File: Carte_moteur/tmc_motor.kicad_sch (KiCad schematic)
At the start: 13 parts, among them J201 Conn_01x05_Pin, J202 Conn_01x04_Pin, SW201 SW_DIP_x02, U201 TMC2209

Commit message: updated motor PCB
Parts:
- removed R205: R_US, Resistor_SMD:R_0603_1608Metric_Pad0.98x0.95mm_HandSolder, symbol Device:R_US
- removed SW201: SW_DIP_x02, Button_Switch_THT:SW_DIP_SPSTx02_Slide_9.78x7.26mm_W7.62mm_P2.54mm, symbol Switch:SW_DIP_x02
- added R210, R211, R212: R_US, Resistor_SMD:R_0603_1608Metric_Pad0.98x0.95mm_HandSolder, symbol Device:R_US
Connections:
- net +3V3: now also R210.2, R211.2, R212.2
- net A: now also R210.1
- net B: now also R211.1
- net I: now also R212.1
- net UART: now also U201.4 (PDN)

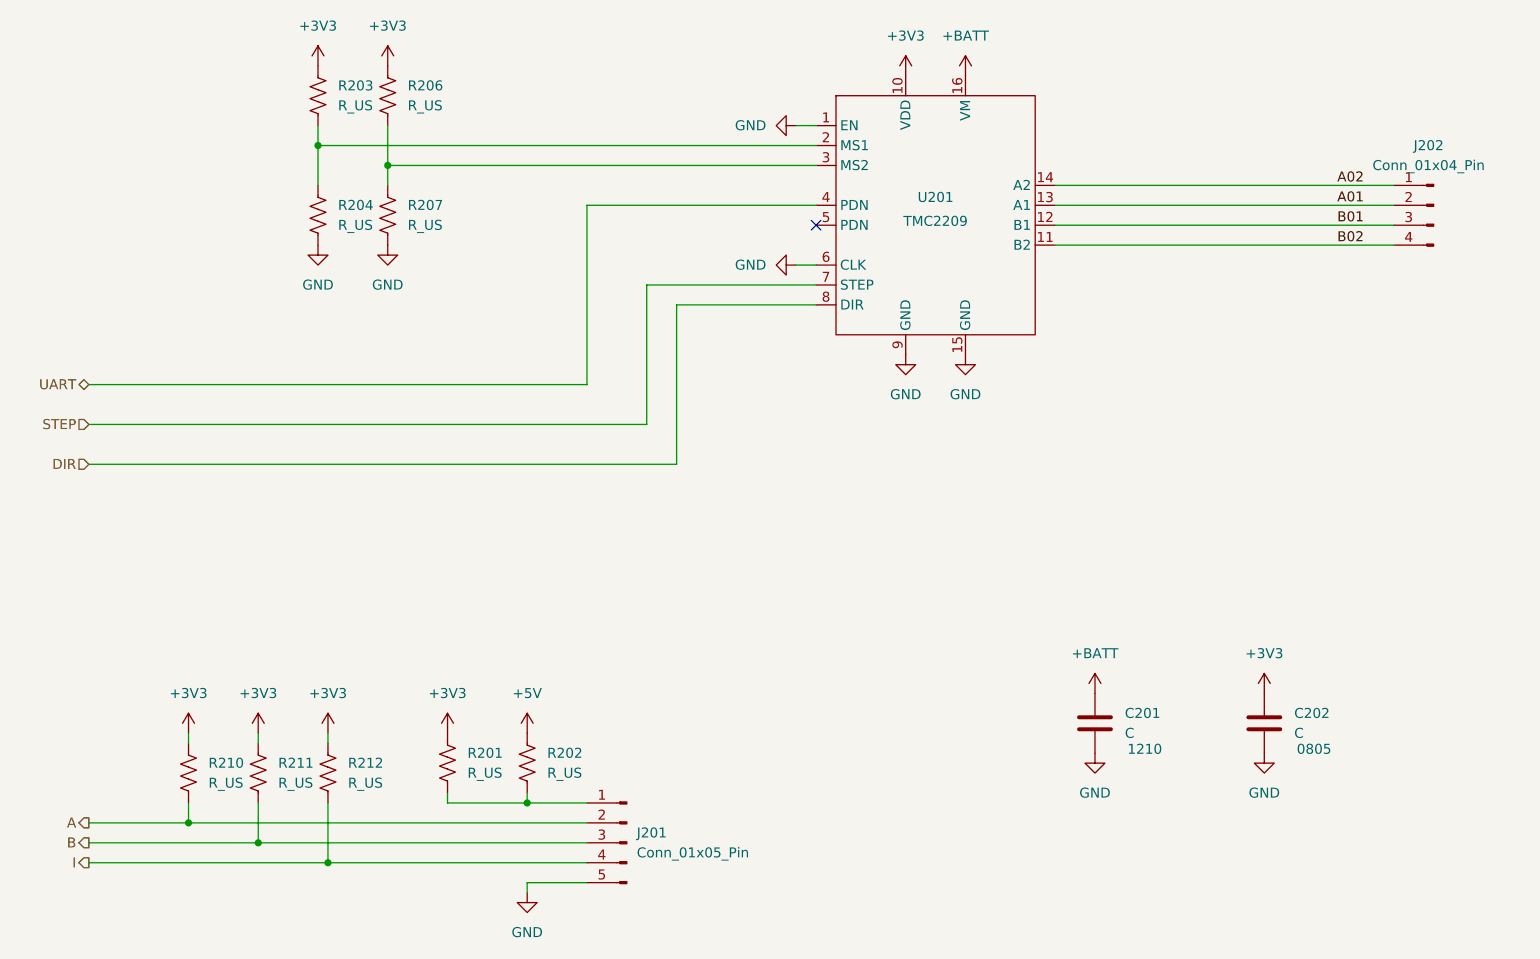
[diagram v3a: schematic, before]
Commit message: update motor board values
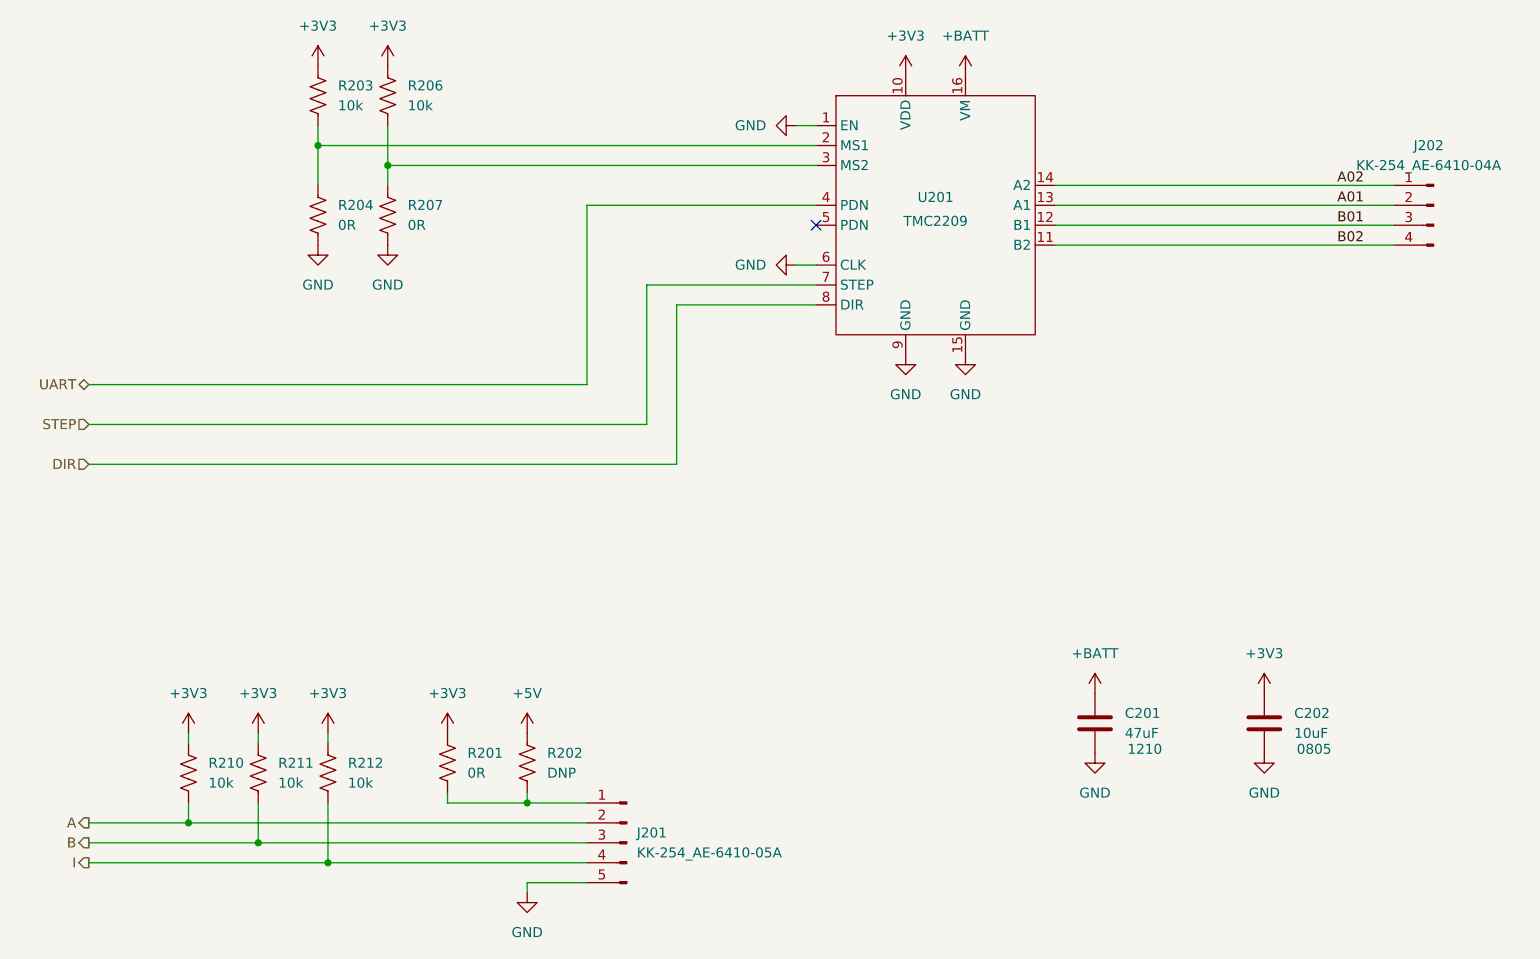
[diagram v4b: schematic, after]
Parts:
- C201: value C -> 47uF
- C202: value C -> 10uF
- J201: value Conn_01x05_Pin -> KK-254_AE-6410-05A
- J202: value Conn_01x04_Pin -> KK-254_AE-6410-04A
- R201, R204, R207: value R_US -> 0R
- R202: value R_US -> DNP
- R203, R206, R210, R211, R212: value R_US -> 10k
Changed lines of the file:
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@@
 			)
 		)
-		(property "Value" "R_US"
+		(property "Value" "10k"
 			(at 72.39 153.6699 0)
 			(effects
@@
 			)
 		)
-		(property "Value" "R_US"
+		(property "Value" "0R"
 			(at 105.41 152.3999 0)
 			(effects
@@
 			)
 		)
-		(property "Value" "R_US"
+		(property "Value" "10k"
 			(at 97.79 67.3099 0)
 			(effects
@@
 			)
 		)
-		(property "Value" "C"
+		(property "Value" "10uF"
 			(at 210.82 147.3199 0)
 			(effects
@@
 			)
 		)
-		(property "Value" "Conn_01x05_Pin"
+		(property "Value" "KK-254_AE-6410-05A"
 			(at 127 162.5599 0)
 			(effects
@@
 			)
 		)
-		(property "Value" "R_US"
+		(property "Value" "0R"
 			(at 97.79 82.5499 0)
 			(effects
@@
 			)
 		)
-		(property "Value" "R_US"
+		(property "Value" "DNP"
 			(at 115.57 152.3999 0)
 			(effects
@@
 			)
 		)
-		(property "Value" "R_US"
+		(property "Value" "0R"
 			(at 88.9 82.5499 0)
 			(effects
@@
 			)
 		)
-		(property "Value" "R_US"
+		(property "Value" "10k"
 			(at 90.17 153.6699 0)
 			(effects
@@
 			)
 		)
-		(property "Value" "C"
+		(property "Value" "47uF"
 			(at 189.23 147.3199 0)
 			(effects
@@
 			)
 		)
-		(property "Value" "R_US"
+		(property "Value" "10k"
 			(at 88.9 67.3099 0)
 			(effects
@@
 			)
 		)
-		(property "Value" "Conn_01x04_Pin"
+		(property "Value" "KK-254_AE-6410-04A"
 			(at 227.965 74.93 0)
 			(effects
@@
 			)
 		)
-		(property "Value" "R_US"
+		(property "Value" "10k"
 			(at 81.28 153.6699 0)
 			(effects
